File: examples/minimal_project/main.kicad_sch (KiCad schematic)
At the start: 1 part, among them U1 STM32F103C8Tx

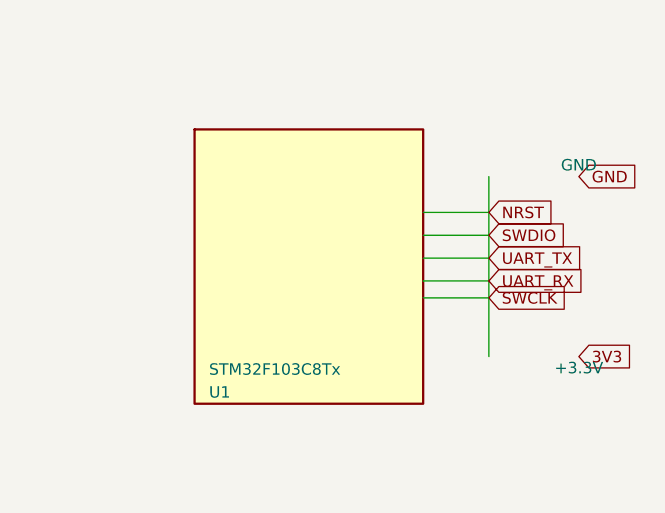
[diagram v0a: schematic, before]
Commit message: feat: complete CLI tests, fix lint errors, and clean up design
- Add comprehensive CLI tests (9 tests) covering inspect, inspect-sch,
  validate, generate, route commands; CLI coverage: 0% -> 85%
- Fix 6 ruff lint errors in tests (unused vars, long lines, unused imports)
- Remove redundant >= 0 checks in _place_fiducials_and_tooling (engine.py)
- Simplify _net_role by removing unused board parameter (drc_repair_agent.py)
- Fix PEP 8 blank line before _run in cli_runner.py
- Overall test coverage: 79% -> 84% (177 tests passing)
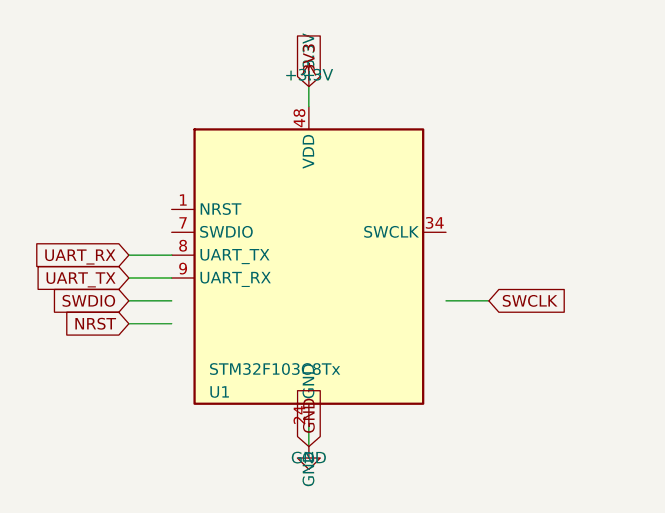
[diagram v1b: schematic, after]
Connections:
- net GND: now also U1.24 (GND)
- new net +3.3V: U1.48 (VDD)
- new net UART_RX: U1.8 (UART_TX)
- new net UART_TX: U1.9 (UART_RX)
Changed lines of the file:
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@@
   (version 20231120)
   (generator "eeschema")
+  (generator_version "8.0")
   (paper "A4")
   (symbol
@@
     (at 100 100 0)
     (unit 1)
+    (exclude_from_sim no)
     (in_bom yes)
     (on_board yes)
+    (dnp no)
     (property "Reference" "U1"
       (at 88.9 113.97 0)
@@
       (effects (font (size 1.27 1.27)) (justify left))
     )
-    (pin "7"  (at 112.7 96.52 0)
-      (effects (font (size 1.27 1.27)))
-    )
-    (pin "34" (at 112.7 103.48 0)
-      (effects (font (size 1.27 1.27)))
-    )
-    (pin "8"  (at 112.7 99.06 0)
-      (effects (font (size 1.27 1.27)))
-    )
-    (pin "9"  (at 112.7 101.6 0)
-      (effects (font (size 1.27 1.27)))
-    )
-    (pin "5"  (at 112.7 93.98 0)
-      (effects (font (size 1.27 1.27)))
-    )
+    (pin "1")
+    (pin "7")
+    (pin "8")
+    (pin "9")
+    (pin "24")
+    (pin "34")
+    (pin "48")
   )
   (symbol
     (lib_id "power:GND")
-    (at 130 90 0)
+    (at 100 120 0)
     (unit 1)
+    (exclude_from_sim no)
     (in_bom yes)
     (on_board yes)
-    (uuid "gnd-001")
+    (dnp no)
+    (uuid "gnd-001-0000-0000-000000000001")
     (property "Reference" "#PWR01"
-      (at 130 86.19 0)
+      (at 100 123.81 0)
       (effects (font (size 1.27 1.27)) hide)
     )
     (property "Value" "GND"
-      (at 130 88.73 0)
+      (at 100 121.27 0)
       (effects (font (size 1.27 1.27)))
     )
+    (pin "1")
   )
   (symbol
     (lib_id "power:+3.3V")
-    (at 130 110 0)
+    (at 100 80 0)
     (unit 1)
+    (exclude_from_sim no)
     (in_bom yes)
     (on_board yes)
-    (uuid "pwr-001")
+    (dnp no)
+    (uuid "pwr-001-0000-0000-000000000001")
     (property "Reference" "#PWR02"
-      (at 130 106.19 0)
+      (at 100 83.81 0)
       (effects (font (size 1.27 1.27)) hide)
     )
     (property "Value" "+3.3V"
-      (at 130 111.27 0)
+      (at 100 78.73 0)
       (effects (font (size 1.27 1.27)))
     )
+    (pin "1")
   )
-  (wire (pts (xy 112.7 96.52) (xy 120 96.52)))
-  (wire (pts (xy 112.7 103.48) (xy 120 103.48)))
-  (wire (pts (xy 112.7 99.06) (xy 120 99.06)))
-  (wire (pts (xy 112.7 101.6) (xy 120 101.6)))
-  (wire (pts (xy 112.7 93.98) (xy 120 93.98)))
-  (wire (pts (xy 120 110) (xy 120 90)))
-  (global_label "SWDIO" (shape input)
-    (at 120 96.52 0)
+  (wire
+    (pts (xy 84.76 106.35) (xy 80 106.35))
+    (stroke (width 0) (type default))
+    (uuid "w0000001-0001-0001-0001-000000000001")
+  )
+  (wire
+    (pts (xy 84.76 103.81) (xy 80 103.81))
+    (stroke (width 0) (type default))
+    (uuid "w0000001-0001-0001-0001-000000000002")
+  )
+  (wire
+    (pts (xy 84.76 101.27) (xy 80 101.27))
+    (stroke (width 0) (type default))
+    (uuid "w0000001-0001-0001-0001-000000000003")
+  )
+  (wire
+    (pts (xy 84.76 98.73) (xy 80 98.73))
+    (stroke (width 0) (type default))
+    (uuid "w0000001-0001-0001-0001-000000000004")
+  )
+  (wire
+    (pts (xy 115.24 103.81) (xy 120 103.81))
+    (stroke (width 0) (type default))
+    (uuid "w0000001-0001-0001-0001-000000000005")
+  )
+  (wire
+    (pts (xy 100 117.78) (xy 100 120))
+    (stroke (width 0) (type default))
+    (uuid "w0000001-0001-0001-0001-000000000006")
+  )
+  (wire
+    (pts (xy 100 82.22) (xy 100 80))
+    (stroke (width 0) (type default))
+    (uuid "w0000001-0001-0001-0001-000000000007")
+  )
+  (global_label "NRST"
+    (shape input)
+    (at 80 106.35 180)
+    (effects (font (size 1.27 1.27)) (justify right))
+    (uuid "gl000001-0001-0001-0001-000000000001")
+  )
+  (global_label "SWDIO"
+    (shape input)
+    (at 80 103.81 180)
+    (effects (font (size 1.27 1.27)) (justify right))
+    (uuid "gl000001-0001-0001-0001-000000000002")
+  )
+  (global_label "UART_TX"
+    (shape input)
+    (at 80 101.27 180)
+    (effects (font (size 1.27 1.27)) (justify right))
+    (uuid "gl000001-0001-0001-0001-000000000003")
+  )
+  (global_label "UART_RX"
+    (shape input)
+    (at 80 98.73 180)
+    (effects (font (size 1.27 1.27)) (justify right))
+    (uuid "gl000001-0001-0001-0001-000000000004")
+  )
+  (global_label "SWCLK"
+    (shape input)
+    (at 120 103.81 0)
     (effects (font (size 1.27 1.27)) (justify left))
+    (uuid "gl000001-0001-0001-0001-000000000005")
   )
-  (global_label "SWCLK" (shape input)
-    (at 120 103.48 0)
+  (global_label "GND"
+    (shape input)
+    (at 100 120 270)
     (effects (font (size 1.27 1.27)) (justify left))
+    (uuid "gl000001-0001-0001-0001-000000000006")
   )
-  (global_label "UART_TX" (shape input)
-    (at 120 99.06 0)
+  (global_label "3V3"
+    (shape input)
+    (at 100 80 90)
     (effects (font (size 1.27 1.27)) (justify left))
-  )
-  (global_label "UART_RX" (shape input)
-    (at 120 101.6 0)
-    (effects (font (size 1.27 1.27)) (justify left))
-  )
-  (global_label "NRST" (shape input)
-    (at 120 93.98 0)
-    (effects (font (size 1.27 1.27)) (justify left))
-  )
-  (global_label "GND" (shape input)
-    (at 130 90 0)
-    (effects (font (size 1.27 1.27)) (justify left))
-  )
-  (global_label "3V3" (shape input)
-    (at 130 110 0)
-    (effects (font (size 1.27 1.27)) (justify left))
+    (uuid "gl000001-0001-0001-0001-000000000007")
   )
 )
